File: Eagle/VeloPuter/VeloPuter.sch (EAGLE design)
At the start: 34 parts, among them IC1 LM2931T-L

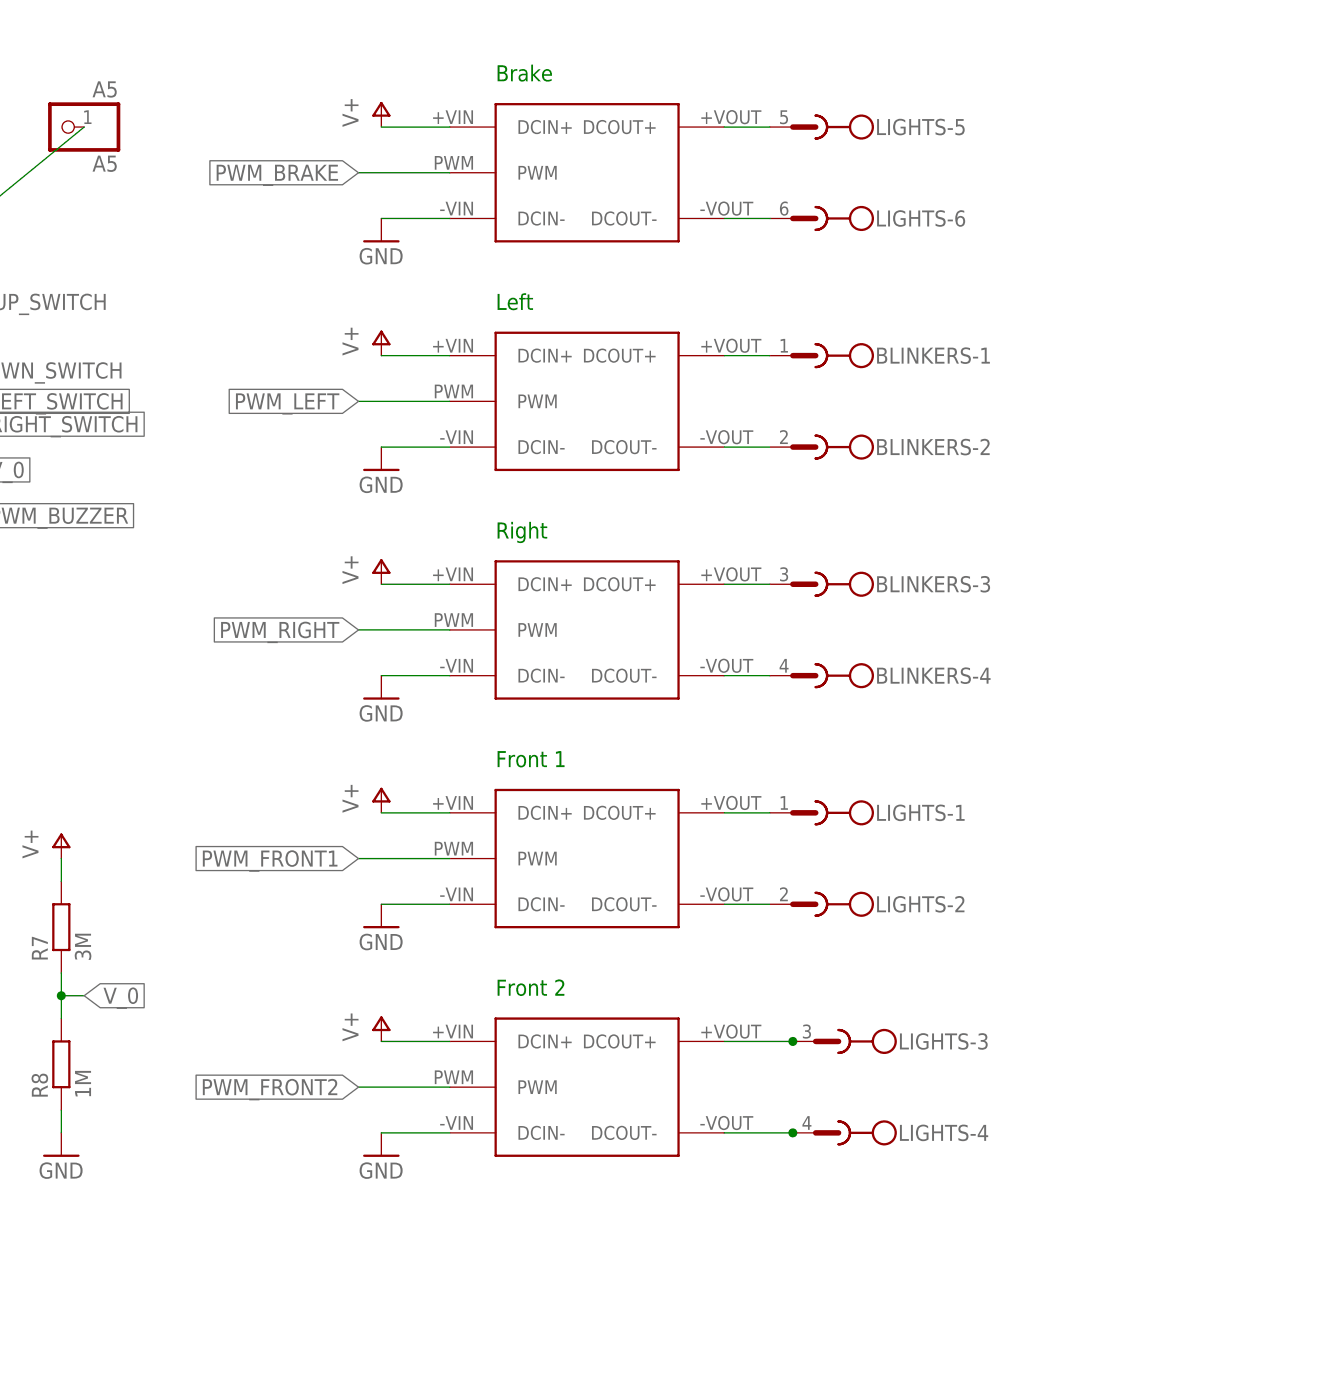
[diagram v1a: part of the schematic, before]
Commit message: Added pulldown resistors for the LDD700 PWM inputs. Without these resistors the LED's would flash brightly before the arduino kicks in.
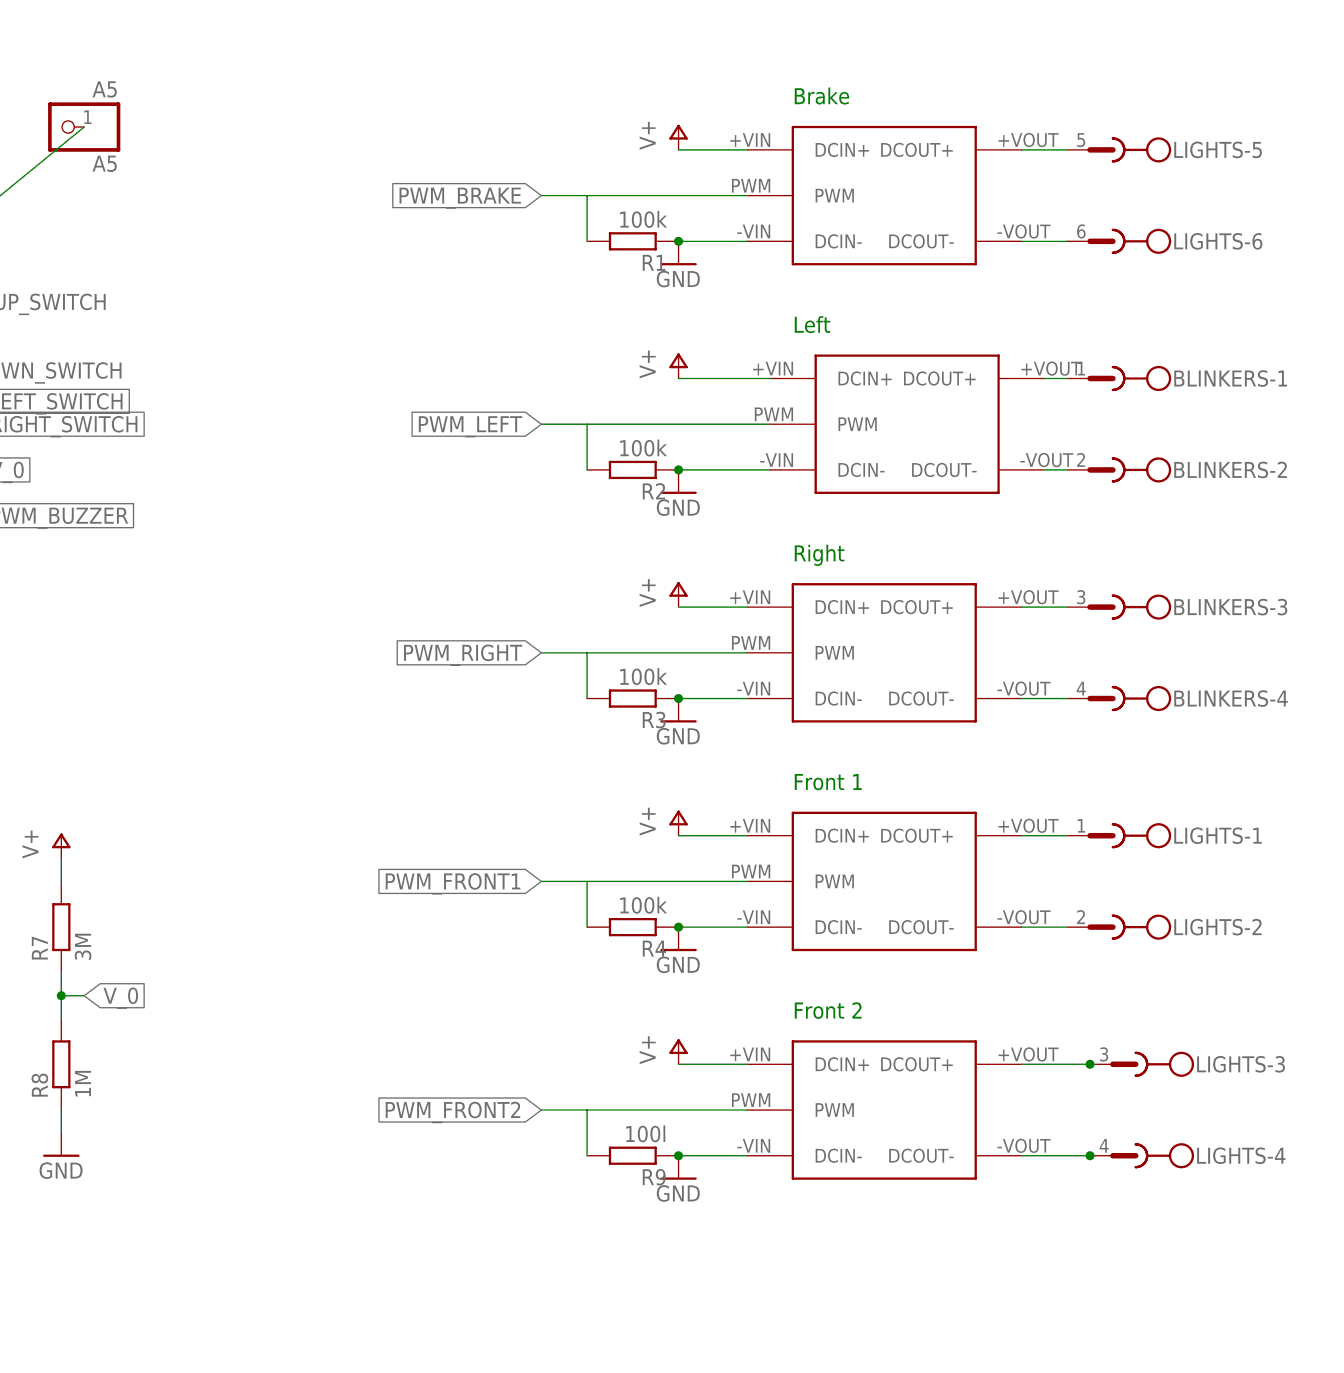
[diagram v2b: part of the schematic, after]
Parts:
- added R1, R2, R3, R4: 100k, resistor:R-EU_0207/10
- added R9: 100l, resistor:R-EU_0207/10
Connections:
- net GND: now also R1.1, R2.1, R3.1, R4.1, R9.1
- net PWM_BRAKE: now also R1.2
- net PWM_FRONT1: now also R4.2
- net PWM_FRONT2: now also R9.2
- net PWM_LEFT: now also R2.2
- net PWM_RIGHT: now also R3.2
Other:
- moved on the sheet: BLINKERS-1, BLINKERS-2, BLINKERS-3, BLINKERS-4, LIGHTS-1, LIGHTS-2, LIGHTS-3, LIGHTS-4, LIGHTS-5, LIGHTS-6

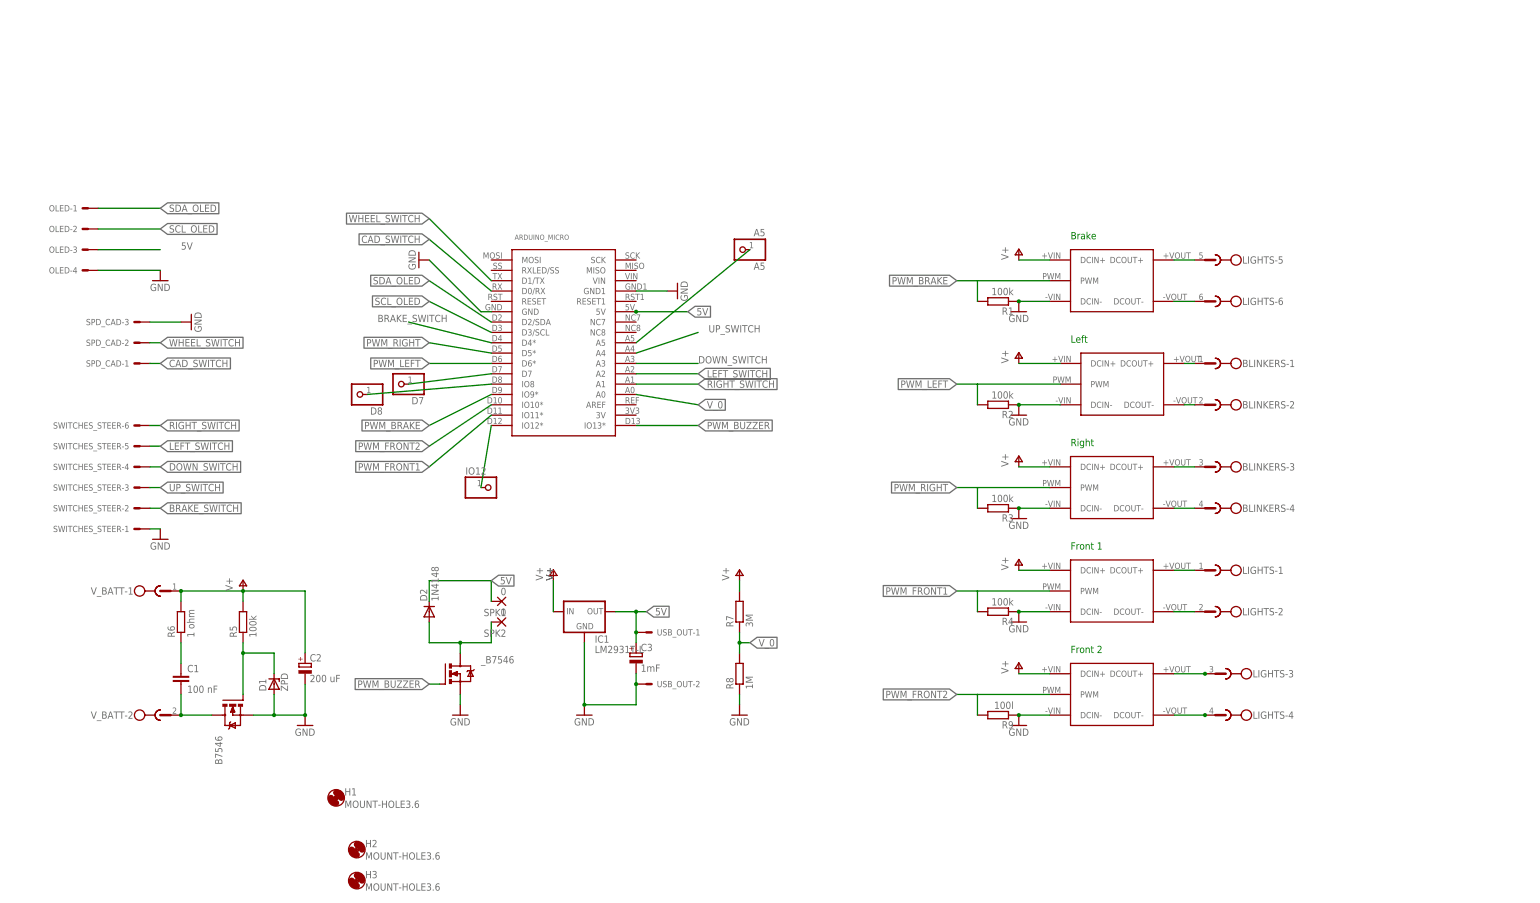
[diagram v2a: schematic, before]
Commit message: new board layout
has to be checked. Pin changes NOT documented
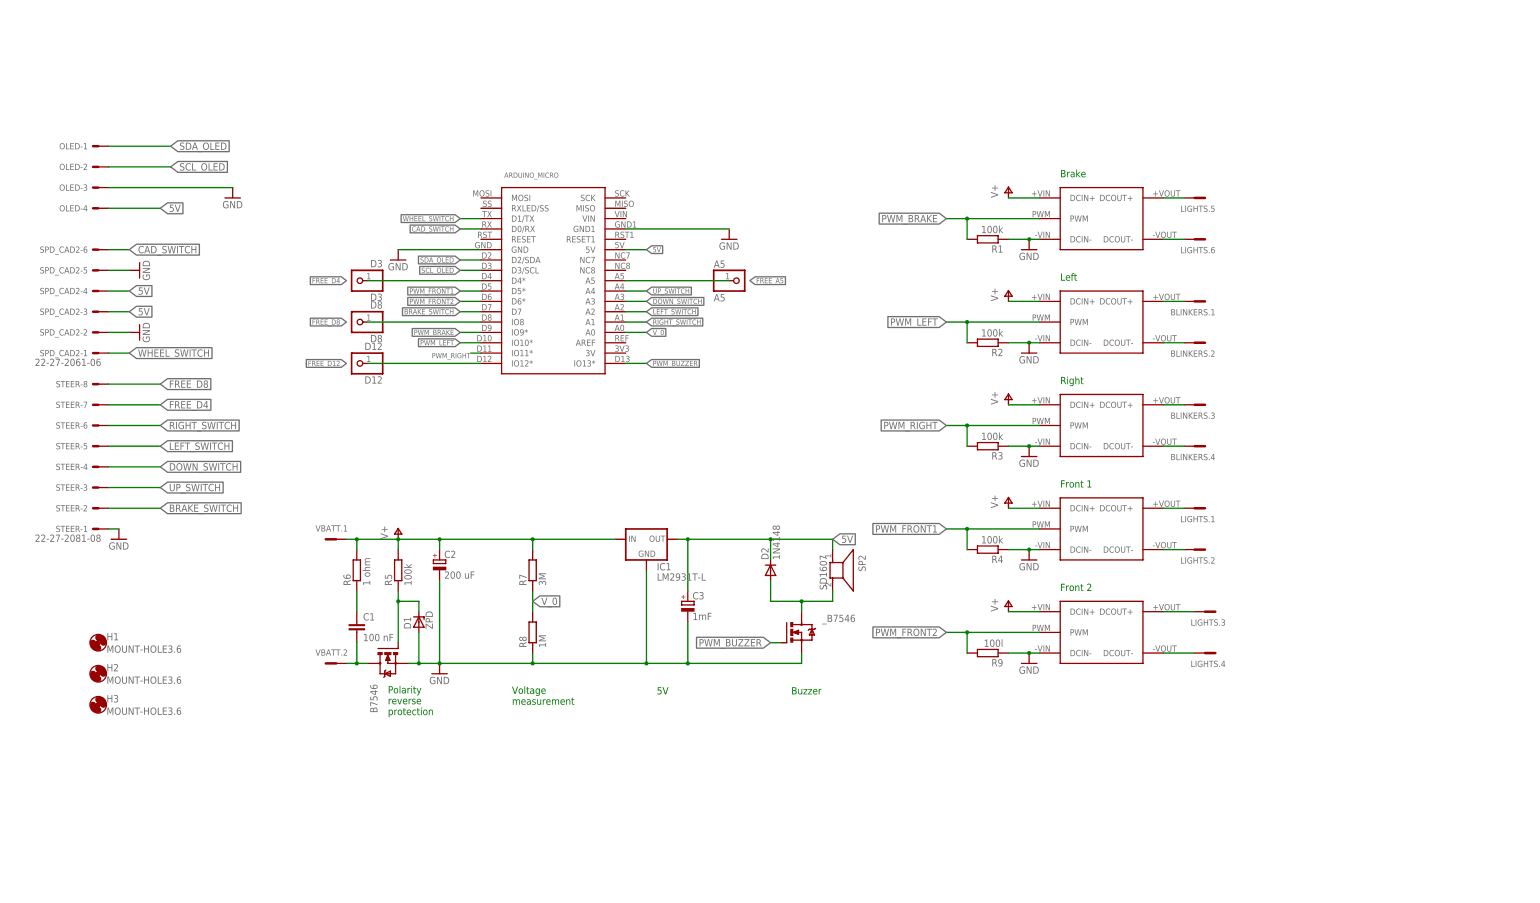
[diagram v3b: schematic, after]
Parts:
- removed D7, IO12: (no value), pinhead:PINHD-1X1
- removed SPD_CAD: 22-27-2031-03, con-molex:22-27-2031-03
- removed SPK1, SPK2: 0, wirepad:2,54/0,8
- removed SWITCHES_STEER: 22-27-2061-06, con-molex:22-27-2061-06
- removed USB_OUT: 22-27-2021-02, con-molex:22-27-2021-02
- removed V_BATT: MSTBV2, con-phoenix-508:MSTBV2
- added D12: D12, pinhead:PINHD-1X1
- added D3: D3, pinhead:PINHD-1X1
- added SP2: SD1607, TDK_SD1607:AL60P
- added SPD_CAD2: 22-27-2061-06, con-molex:22-27-2061-06
- added STEER: 22-27-2081-08, con-molex:22-27-2081-08
- added VBATT: MCV2, con-phoenix_3.81_mcv:MCV2
- BLINKERS: value MSTBV4 -> 0; device con-phoenix-508:MSTBV4 -> con-phoenix_3.81_mcv:MCV4
- D8: value (none) -> D8
- LIGHTS: value MSTBV6 -> 0; device con-phoenix-508:MSTBV6 -> con-phoenix_3.81_mcv:MCV6
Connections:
- net A5 renamed FREE_A5
- removed net IO12: ARDUINO_MICRO.IO12*, IO12.1
- removed net N$16: ARDUINO_MICRO.D7, D7.1
- removed net N$17: ARDUINO_MICRO.IO8, D8.1
- new net FREE_D12: ARDUINO_MICRO.IO12*, D12.1
- new net FREE_D4: ARDUINO_MICRO.D4*, D3.1, STEER-7.S
- new net FREE_D8: ARDUINO_MICRO.IO8, D8.1, STEER-8.S
- net 5V: now also OLED-4.S, SP2.1, SPD_CAD2-3.S, SPD_CAD2-4.S; no longer OLED-3.S, SPK1.P, USB_OUT-1.S
- net BRAKE_SWITCH: now also ARDUINO_MICRO.D7, STEER-2.S; no longer ARDUINO_MICRO.D4*, SWITCHES_STEER-2.S
- net CAD_SWITCH: now also SPD_CAD2-6.S; no longer SPD_CAD-1.S
- net DOWN_SWITCH: now also STEER-4.S; no longer SWITCHES_STEER-4.S
- net GND: now also OLED-3.S, SPD_CAD2-2.S, SPD_CAD2-5.S, STEER-1.S; no longer OLED-4.S, SPD_CAD-3.S, SWITCHES_STEER-1.S, USB_OUT-2.S
- net LEFT_SWITCH: now also STEER-5.S; no longer SWITCHES_STEER-5.S
- net N$10: now also LIGHTS.1.SK; no longer LIGHTS-1.1
- net N$11: now also LIGHTS.2.SK; no longer LIGHTS-2.1
- net N$12: now also LIGHTS.3.SK; no longer LIGHTS-3.1
- net N$13: now also LIGHTS.4.SK; no longer LIGHTS-4.1
- net N$14: now also SP2.2; no longer SPK2.P
- net N$2: now also VBATT.2.SK; no longer V_BATT-2.1
- net N$3: now also LIGHTS.5.SK; no longer LIGHTS-5.1
- net N$5: now also LIGHTS.6.SK; no longer LIGHTS-6.1
- net N$6: now also BLINKERS.1.SK; no longer BLINKERS-1.1
- net N$7: now also BLINKERS.2.SK; no longer BLINKERS-2.1
- net N$8: now also BLINKERS.3.SK; no longer BLINKERS-3.1
- net N$9: now also BLINKERS.4.SK; no longer BLINKERS-4.1
- net PWM_FRONT1: now also ARDUINO_MICRO.D5*; no longer ARDUINO_MICRO.IO11*
- net PWM_FRONT2: now also ARDUINO_MICRO.D6*; no longer ARDUINO_MICRO.IO10*
- net PWM_LEFT: now also ARDUINO_MICRO.IO10*; no longer ARDUINO_MICRO.D6*
- net PWM_RIGHT: now also ARDUINO_MICRO.IO11*; no longer ARDUINO_MICRO.D5*
- net RIGHT_SWITCH: now also STEER-6.S; no longer SWITCHES_STEER-6.S
- net UP_SWITCH: now also STEER-3.S; no longer SWITCHES_STEER-3.S
- net V+: now also VBATT.1.SK; no longer V_BATT-1.1
- net WHEEL_SWITCH: now also SPD_CAD2-1.S; no longer SPD_CAD-2.S
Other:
- note added: "5V"
- note added: "Buzzer"
- note added: "Polarity reverse protection"
- note added: "Voltage measurement"
- moved on the sheet: A5, ARDUINO_MICRO, B7546, C1, C2, C3, D1, D2, D8, H1, H2, H3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

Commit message: Version of the Veloputer PCB as made as version 1.2 (number of the PCB).
This version is uploaded to seeedstudio.com on 2016-02-21.
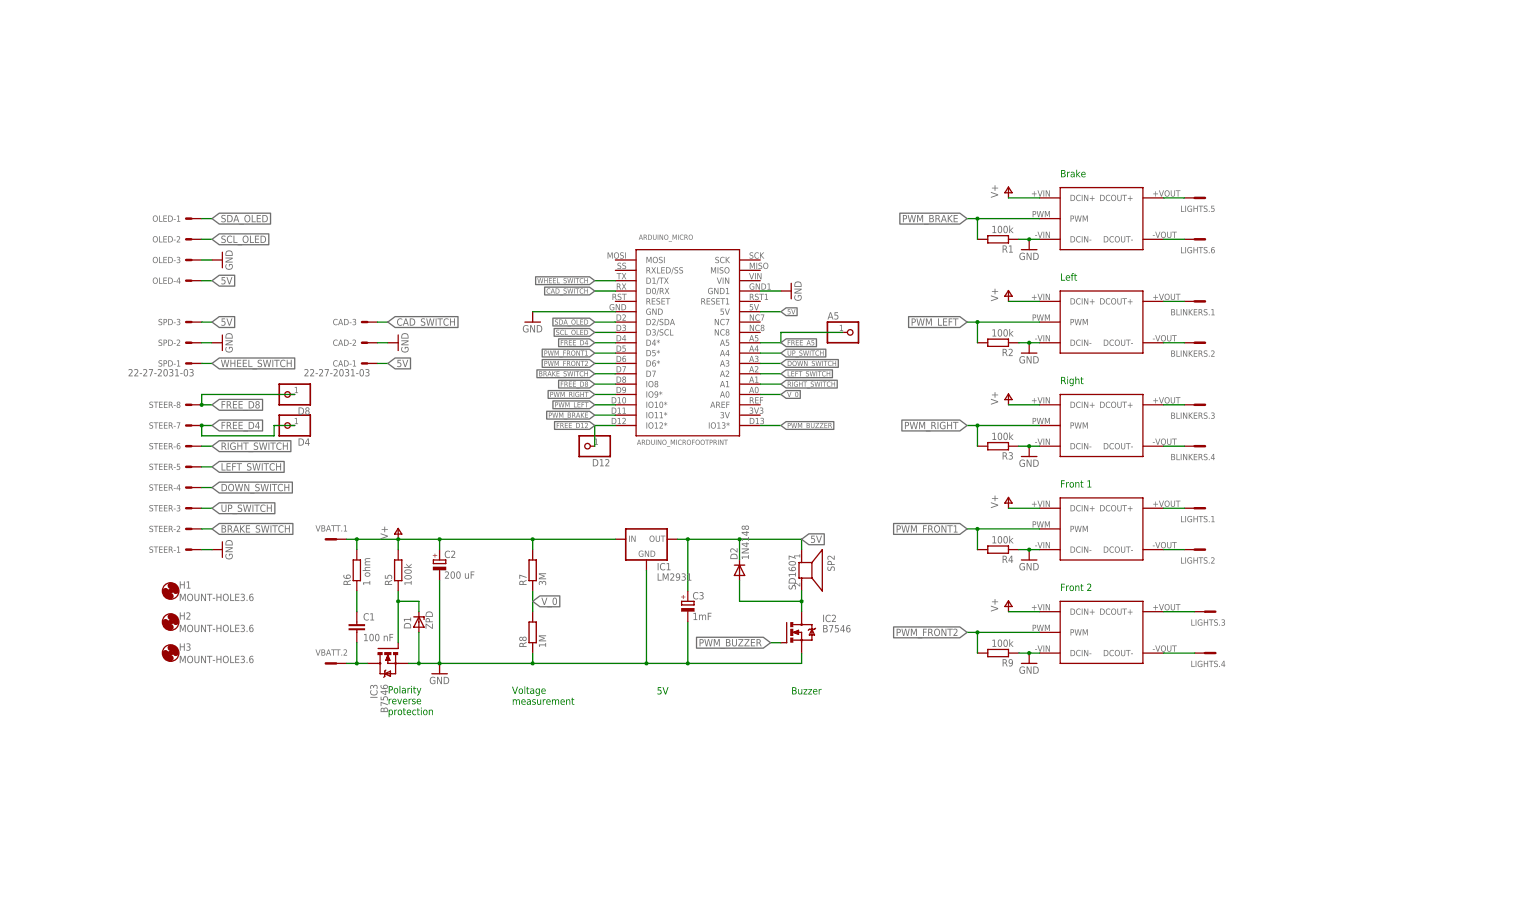
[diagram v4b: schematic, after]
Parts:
- removed D3: D3, pinhead:PINHD-1X1
- removed SPD_CAD2: 22-27-2061-06, con-molex:22-27-2061-06
- added CAD, SPD: 22-27-2031-03, con-molex:22-27-2031-03
- added D4: (no value), pinhead:PINHD-1X1
- A5: value A5 -> (none)
- ARDUINO_MICRO: device arduino-micro:ARDUINO_MICROFOOTPRINT -> arduino-micro_gbeu:ARDUINO_MICROFOOTPRINT
- BLINKERS, LIGHTS: value 0 -> (none)
- C3: device resistor:CPOL-EUE5-13 -> resistor:CPOL-EUE5-10.5
- D12: value D12 -> (none)
- D2: device diode:1N4004 -> diode:1N4148DO35-7
- D8: value D8 -> (none)
- IC1: value LM2931T-L -> LM2931; device v-reg-3:LM2931T-L -> v-reg-3-gbeu:LM2931T-L
- IC2, IC3: value IRFZ48Z -> B7546
- R9: value 100l -> 100k
- VBATT: value MCV2 -> (none)
- renumbered B7546 to IC3, _B7546 to IC2
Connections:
- net N$2 renamed V-
- net 5V: now also CAD-1.S, SPD-3.S; no longer SPD_CAD2-3.S, SPD_CAD2-4.S
- net CAD_SWITCH: now also CAD-3.S; no longer SPD_CAD2-6.S
- net FREE_D4: now also D4.1; no longer D3.1
- net GND: now also CAD-2.S, SPD-2.S; no longer SPD_CAD2-2.S, SPD_CAD2-5.S
- net PWM_BRAKE: now also ARDUINO_MICRO.IO11*; no longer ARDUINO_MICRO.IO9*
- net PWM_RIGHT: now also ARDUINO_MICRO.IO9*; no longer ARDUINO_MICRO.IO11*
- net WHEEL_SWITCH: now also SPD-1.S; no longer SPD_CAD2-1.S
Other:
- moved on the sheet: A5, ARDUINO_MICRO, D12, D8, H1, H2, H3, OLED-1, OLED-2, OLED-3, OLED-4, R1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
